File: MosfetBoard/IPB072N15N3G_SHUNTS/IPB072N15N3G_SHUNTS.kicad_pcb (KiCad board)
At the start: 2 copper layers, 147 x 97 mm, 116 parts, among them J1 DRIVER1, J13 BATT+Conn2, J14 BATT-Conn2, J15 PHASE_PAD, J16 PHASE_PAD, J2 DRIVER2, J3 DRIVER3, J4 PhaseConn1, J5 PhaseConn2, J6 PhaseConn3, J7 PHASE_PAD, J8 BATT+Conn1, J9 BATT-Conn1, Q1 IPB072N15N3G, Q10 IPB072N15N3G, Q11 IPB072N15N3G, Q12 IPB072N15N3G, Q2 IPB072N15N3G, Q3 IPB072N15N3G, Q4 IPB072N15N3G, Q5 IPB072N15N3G, Q6 IPB072N15N3G, Q7 IPB072N15N3G, Q8 IPB072N15N3G, Q9 IPB072N15N3G, U1 RS2166XC5, U4 NCS2003ASN2T1G, U5 RS2166XC5, U7 RS2166XC5, U8 NCS2003ASN2T1G, U9 NCS2003ASN2T1G

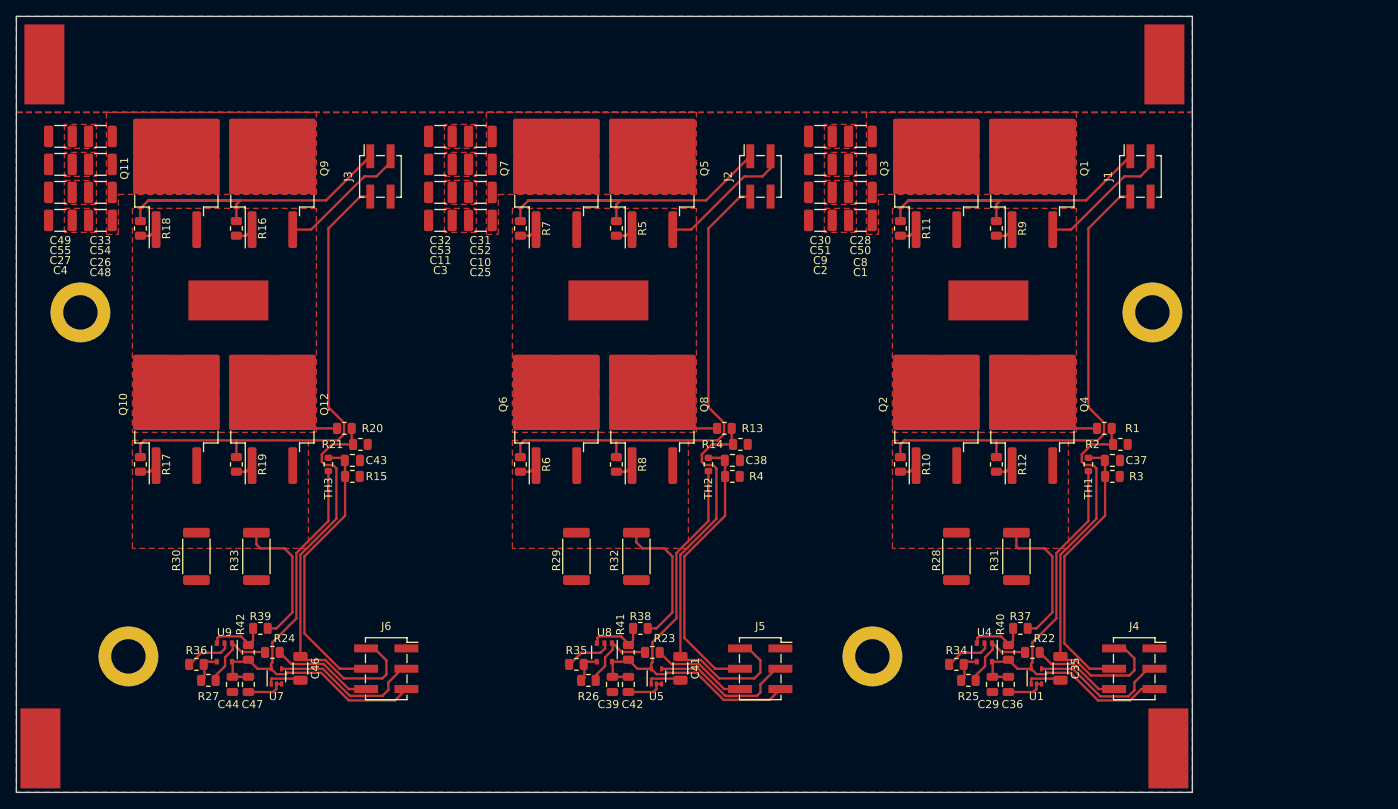
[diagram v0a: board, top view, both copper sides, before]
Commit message: fixing_giga_mistake
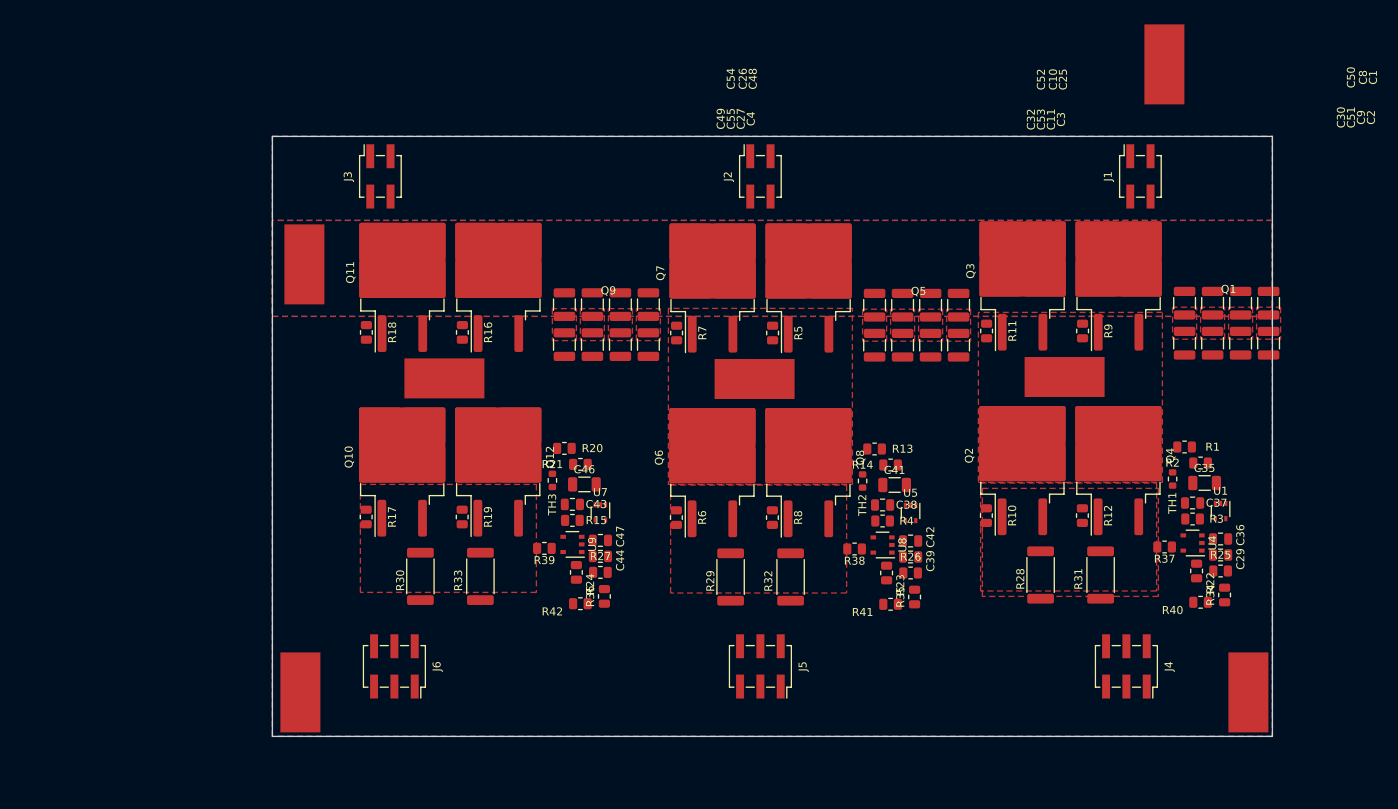
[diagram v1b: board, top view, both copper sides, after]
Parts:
- removed H1, H2, H3, H4: MountingHole, MountingHole:MountingHole_4.3mm_M4_DIN965_Pad
- J2: value DRIVER2 -> DRIVER1
- J3: value DRIVER3 -> DRIVER1
- J4: value PhaseConn1 -> PhaseConn
- J5: value PhaseConn2 -> PhaseConn
- J6: value PhaseConn3 -> PhaseConn
- moved C4 75.1 mm to (142.0, 79.0), turned to -90 degrees
- moved C27 72.5 mm to (138.5, 79.0), turned to -90 degrees
- moved C55 70.2 mm to (135.0, 79.0), turned to -90 degrees
- moved C48 69.3 mm to (142.0, 74.0), turned to -90 degrees
- moved C49 68.2 mm to (131.5, 79.0), turned to -90 degrees
- moved C3 66.6 mm to (180.8, 79.1), turned to -90 degrees
- moved C26 66.5 mm to (138.5, 74.0), turned to -90 degrees
- moved C11 64.2 mm to (177.3, 79.1), turned to -90 degrees
- moved C54 63.9 mm to (135.0, 74.0), turned to -90 degrees
- moved C53 62.0 mm to (173.8, 79.1), turned to -90 degrees
- moved C33 61.7 mm to (131.5, 74.0), turned to -90 degrees
- moved C25 60.7 mm to (180.8, 74.1), turned to -90 degrees
- moved C32 60.2 mm to (170.3, 79.1), turned to -90 degrees
- moved C2 58.1 mm to (219.5, 78.8), turned to -90 degrees
- moved C10 58.0 mm to (177.3, 74.1), turned to -90 degrees
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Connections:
- net 3.3V_1 renamed /PhaseMosfets/3.3V_IN
- net 3.3V_2 renamed /PhaseMosfets1/3.3V_IN
- net 3.3V_3 renamed /PhaseMosfets2/3.3V_IN
- net CURR1 renamed /PhaseMosfets/CURRENT_SENSE
- net CURR2 renamed /PhaseMosfets1/CURRENT_SENSE
- net CURR3 renamed /PhaseMosfets2/CURRENT_SENSE
- net MOSTEMP1 renamed /PhaseMosfets/MOS_TEMP
- net MOSTEMP2 renamed /PhaseMosfets1/MOS_TEMP
- net MOSTEMP3 renamed /PhaseMosfets2/MOS_TEMP
- net PH1 renamed /PhaseMosfets/PH
- net PH2 renamed /PhaseMosfets1/PH
- net PH3 renamed /PhaseMosfets2/PH
- net PHASE1 renamed /PhaseMosfets/PHASE
- net PHASE2 renamed /PhaseMosfets1/PHASE
- net PHASE3 renamed /PhaseMosfets2/PHASE
- net PL1 renamed /PhaseMosfets/PL
- net PL2 renamed /PhaseMosfets1/PL
- net PL3 renamed /PhaseMosfets2/PL
- net SENS_FILTER_ENABLE1 renamed /PhaseMosfets/SENSE_FILTER_EN
- net SENS_FILTER_ENABLE2 renamed /PhaseMosfets1/SENSE_FILTER_EN
- net SENS_FILTER_ENABLE3 renamed /PhaseMosfets2/SENSE_FILTER_EN
- net VSENSE1 renamed /PhaseMosfets/V_SENSE
- net VSENSE2 renamed /PhaseMosfets1/V_SENSE
- net VSENSE3 renamed /PhaseMosfets2/V_SENSE
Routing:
- net /PhaseMosfets2/PL: track 63.0 -> 0.00 mm
- net /PhaseMosfets1/PL: track 63.0 -> 0.00 mm
- net /PhaseMosfets/PL: track 63.0 -> 0.00 mm
- net /PhaseMosfets2/3.3V_IN: track 56.3 -> 0.00 mm
- net /PhaseMosfets1/3.3V_IN: track 55.5 -> 0.00 mm
- net /PhaseMosfets/3.3V_IN: track 54.8 -> 0.00 mm
- net /PhaseMosfets2/V_SENSE: track 51.2 -> 0.00 mm
- net /PhaseMosfets1/V_SENSE: track 50.3 -> 0.00 mm
- net /PhaseMosfets/V_SENSE: track 49.3 -> 0.00 mm
- net /PhaseMosfets2/PH: track 47.3 -> 0.00 mm
- net /PhaseMosfets1/PH: track 47.3 -> 0.00 mm
- net /PhaseMosfets/PH: track 47.3 -> 0.00 mm
- net /PhaseMosfets1/MOS_TEMP: track 35.8 -> 0.00 mm
- net /PhaseMosfets2/MOS_TEMP: track 35.5 -> 0.00 mm
- net /PhaseMosfets/MOS_TEMP: track 33.7 -> 0.00 mm
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- removed copper zone on F.Cu, net /PhaseMosfets2/PHASE
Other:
- board size 147 x 97 mm -> 125 x 75 mm

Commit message: fixeddimensions
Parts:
- moved C28 14.2 mm to (208.8, 88.0), turned to 0 degrees
- moved C33 14.1 mm to (133.0, 88.0), turned to 0 degrees
- moved C31 13.9 mm to (169.8, 88.0), turned to 0 degrees
- moved C25 11.5 mm to (169.8, 77.5), turned to 0 degrees
- moved C1 11.4 mm to (208.8, 77.5), turned to 0 degrees
- moved C50 11.3 mm to (208.8, 84.5), turned to 0 degrees
- moved C52 11.2 mm to (169.8, 84.5), turned to 0 degrees
- moved C49 11.1 mm to (138.0, 88.0), turned to 0 degrees
- moved C54 10.7 mm to (133.0, 84.5), turned to 0 degrees
- moved C30 10.3 mm to (213.8, 88.0), turned to 0 degrees
- moved C10 10.2 mm to (169.8, 81.0), turned to 0 degrees
- moved C8 10.2 mm to (208.8, 81.0), turned to 0 degrees
- moved C32 9.96 mm to (174.8, 88.0), turned to 0 degrees
- moved C48 9.65 mm to (133.0, 77.5), turned to 0 degrees
- moved C26 8.88 mm to (133.0, 81.0), turned to 0 degrees
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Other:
- board size 125 x 75 mm -> 115 x 75 mm

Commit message: movedconnectors
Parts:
- moved J13 29.1 mm to (211.2, 72.8)
- moved Q1 7.91 mm to (192.5, 74.5)
- moved R9 7.91 mm to (188.0, 82.0)
- moved Q4 7.70 mm to (192.5, 97.2)
- moved R12 7.70 mm to (188.0, 104.8)
- moved R30 7.60 mm to (119.0, 113.2)
- moved C50 7.59 mm to (201.5, 86.8)
- moved C2 7.59 mm to (206.5, 79.8)
- moved C30 7.59 mm to (206.5, 90.2)
- moved C51 7.59 mm to (206.5, 86.8)
- moved C8 7.59 mm to (201.5, 83.2)
- moved C9 7.59 mm to (206.5, 83.2)
- moved C28 7.59 mm to (201.5, 90.2)
- moved C1 7.59 mm to (201.5, 79.8)
- moved Q3 7.50 mm to (181.0, 74.5)
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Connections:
- C29 pad 1: /PhaseMosfets/3.3V_IN -> /PhaseMosfets1/3.3V_IN
- C35 pad 1: /PhaseMosfets/V_SENSE -> /PhaseMosfets1/V_SENSE
- C36 pad 1: /PhaseMosfets/3.3V_IN -> /PhaseMosfets1/3.3V_IN
- C37 pad 1: /PhaseMosfets/MOS_TEMP -> /PhaseMosfets1/MOS_TEMP
- C38 pad 1: /PhaseMosfets1/MOS_TEMP -> /PhaseMosfets2/MOS_TEMP
- C39 pad 1: /PhaseMosfets1/3.3V_IN -> /PhaseMosfets2/3.3V_IN
- C41 pad 1: /PhaseMosfets1/V_SENSE -> /PhaseMosfets2/V_SENSE
- C42 pad 1: /PhaseMosfets1/3.3V_IN -> /PhaseMosfets2/3.3V_IN
- C43 pad 1: /PhaseMosfets2/MOS_TEMP -> /PhaseMosfets3/MOS_TEMP
- C44 pad 1: /PhaseMosfets2/3.3V_IN -> /PhaseMosfets3/3.3V_IN
- C46 pad 1: /PhaseMosfets2/V_SENSE -> /PhaseMosfets3/V_SENSE
- C47 pad 1: /PhaseMosfets2/3.3V_IN -> /PhaseMosfets3/3.3V_IN
- J1 pad 1: /PhaseMosfets/PH -> /PhaseMosfets1/PH
- J1 pad 2: /PhaseMosfets/PL -> /PhaseMosfets1/PL
- J1 pad 3: /PhaseMosfets/PHASE -> /PhaseMosfets1/PHASE
- J15 pad 1: /PhaseMosfets1/PHASE -> /PhaseMosfets2/PHASE
- J16 pad 1: /PhaseMosfets2/PHASE -> /PhaseMosfets3/PHASE
- J2 pad 1: /PhaseMosfets1/PH -> /PhaseMosfets2/PH
- J2 pad 2: /PhaseMosfets1/PL -> /PhaseMosfets2/PL
- J2 pad 3: /PhaseMosfets1/PHASE -> /PhaseMosfets2/PHASE
- J3 pad 1: /PhaseMosfets2/PH -> /PhaseMosfets3/PH
- J3 pad 2: /PhaseMosfets2/PL -> /PhaseMosfets3/PL
- J3 pad 3: /PhaseMosfets2/PHASE -> /PhaseMosfets3/PHASE
- J4 pad 2: /PhaseMosfets/V_SENSE -> /PhaseMosfets1/V_SENSE
- J4 pad 3: /PhaseMosfets/SENSE_FILTER_EN -> /PhaseMosfets1/SENSE_FILTER_EN
- J4 pad 4: /PhaseMosfets/MOS_TEMP -> /PhaseMosfets1/MOS_TEMP
- J4 pad 5: /PhaseMosfets/3.3V_IN -> /PhaseMosfets1/3.3V_IN
- J4 pad 6: /PhaseMosfets/CURRENT_SENSE -> /PhaseMosfets1/CURRENT_SENSE
- J5 pad 2: /PhaseMosfets1/V_SENSE -> /PhaseMosfets2/V_SENSE
- J5 pad 3: /PhaseMosfets1/SENSE_FILTER_EN -> /PhaseMosfets2/SENSE_FILTER_EN
- J5 pad 4: /PhaseMosfets1/MOS_TEMP -> /PhaseMosfets2/MOS_TEMP
- J5 pad 5: /PhaseMosfets1/3.3V_IN -> /PhaseMosfets2/3.3V_IN
- J5 pad 6: /PhaseMosfets1/CURRENT_SENSE -> /PhaseMosfets2/CURRENT_SENSE
- J6 pad 2: /PhaseMosfets2/V_SENSE -> /PhaseMosfets3/V_SENSE
- J6 pad 3: /PhaseMosfets2/SENSE_FILTER_EN -> /PhaseMosfets3/SENSE_FILTER_EN
- J6 pad 4: /PhaseMosfets2/MOS_TEMP -> /PhaseMosfets3/MOS_TEMP
- J6 pad 5: /PhaseMosfets2/3.3V_IN -> /PhaseMosfets3/3.3V_IN
- J6 pad 6: /PhaseMosfets2/CURRENT_SENSE -> /PhaseMosfets3/CURRENT_SENSE
- J7 pad 1: /PhaseMosfets/PHASE -> /PhaseMosfets1/PHASE
- Q1 pad 3: /PhaseMosfets/PHASE -> /PhaseMosfets1/PHASE
- Q10 pad 2: /PhaseMosfets2/PHASE -> /PhaseMosfets3/PHASE
- Q10 pad 3: /PhaseMosfets2/SH+ -> /PhaseMosfets3/SH+
- Q11 pad 3: /PhaseMosfets2/PHASE -> /PhaseMosfets3/PHASE
- Q12 pad 2: /PhaseMosfets2/PHASE -> /PhaseMosfets3/PHASE
- Q12 pad 3: /PhaseMosfets2/SH+ -> /PhaseMosfets3/SH+
- Q2 pad 2: /PhaseMosfets/PHASE -> /PhaseMosfets1/PHASE
- Q2 pad 3: /PhaseMosfets/SH+ -> /PhaseMosfets1/SH+
- Q3 pad 3: /PhaseMosfets/PHASE -> /PhaseMosfets1/PHASE
- Q4 pad 2: /PhaseMosfets/PHASE -> /PhaseMosfets1/PHASE
- Q4 pad 3: /PhaseMosfets/SH+ -> /PhaseMosfets1/SH+
- Q5 pad 3: /PhaseMosfets1/PHASE -> /PhaseMosfets2/PHASE
- Q6 pad 2: /PhaseMosfets1/PHASE -> /PhaseMosfets2/PHASE
- Q6 pad 3: /PhaseMosfets1/SH+ -> /PhaseMosfets2/SH+
- Q7 pad 3: /PhaseMosfets1/PHASE -> /PhaseMosfets2/PHASE
- Q8 pad 2: /PhaseMosfets1/PHASE -> /PhaseMosfets2/PHASE
- Q8 pad 3: /PhaseMosfets1/SH+ -> /PhaseMosfets2/SH+
- Q9 pad 3: /PhaseMosfets2/PHASE -> /PhaseMosfets3/PHASE
- R1 pad 1: /PhaseMosfets/PHASE -> /PhaseMosfets1/PHASE
- R1 pad 2: /PhaseMosfets/V_SENSE -> /PhaseMosfets1/V_SENSE
- R10 pad 1: /PhaseMosfets/PL -> /PhaseMosfets1/PL
- R11 pad 1: /PhaseMosfets/PH -> /PhaseMosfets1/PH
- R12 pad 1: /PhaseMosfets/PL -> /PhaseMosfets1/PL
- R13 pad 1: /PhaseMosfets1/PHASE -> /PhaseMosfets2/PHASE
- R13 pad 2: /PhaseMosfets1/V_SENSE -> /PhaseMosfets2/V_SENSE
- R14 pad 1: /PhaseMosfets1/V_SENSE -> /PhaseMosfets2/V_SENSE
- R15 pad 1: /PhaseMosfets2/MOS_TEMP -> /PhaseMosfets3/MOS_TEMP
- R16 pad 1: /PhaseMosfets2/PH -> /PhaseMosfets3/PH
- R17 pad 1: /PhaseMosfets2/PL -> /PhaseMosfets3/PL
- R18 pad 1: /PhaseMosfets2/PH -> /PhaseMosfets3/PH
- R19 pad 1: /PhaseMosfets2/PL -> /PhaseMosfets3/PL
- R2 pad 1: /PhaseMosfets/V_SENSE -> /PhaseMosfets1/V_SENSE
- R20 pad 1: /PhaseMosfets2/PHASE -> /PhaseMosfets3/PHASE
- R20 pad 2: /PhaseMosfets2/V_SENSE -> /PhaseMosfets3/V_SENSE
- R21 pad 1: /PhaseMosfets2/V_SENSE -> /PhaseMosfets3/V_SENSE
- R22 pad 2: /PhaseMosfets/CURRENT_SENSE -> /PhaseMosfets1/CURRENT_SENSE
- R23 pad 2: /PhaseMosfets1/CURRENT_SENSE -> /PhaseMosfets2/CURRENT_SENSE
- R24 pad 2: /PhaseMosfets2/CURRENT_SENSE -> /PhaseMosfets3/CURRENT_SENSE
- R28 pad 1: /PhaseMosfets/SH+ -> /PhaseMosfets1/SH+
- R29 pad 1: /PhaseMosfets1/SH+ -> /PhaseMosfets2/SH+
- R3 pad 1: /PhaseMosfets/MOS_TEMP -> /PhaseMosfets1/MOS_TEMP
- R30 pad 1: /PhaseMosfets2/SH+ -> /PhaseMosfets3/SH+
- R31 pad 1: /PhaseMosfets/SH+ -> /PhaseMosfets1/SH+
- R32 pad 1: /PhaseMosfets1/SH+ -> /PhaseMosfets2/SH+
- R33 pad 1: /PhaseMosfets2/SH+ -> /PhaseMosfets3/SH+
- R37 pad 1: /PhaseMosfets/SH+ -> /PhaseMosfets1/SH+
- R38 pad 1: /PhaseMosfets1/SH+ -> /PhaseMosfets2/SH+
- R39 pad 1: /PhaseMosfets2/SH+ -> /PhaseMosfets3/SH+
- R4 pad 1: /PhaseMosfets1/MOS_TEMP -> /PhaseMosfets2/MOS_TEMP
- R40 pad 1: /PhaseMosfets/3.3V_IN -> /PhaseMosfets1/3.3V_IN
- R41 pad 1: /PhaseMosfets1/3.3V_IN -> /PhaseMosfets2/3.3V_IN
- R42 pad 1: /PhaseMosfets2/3.3V_IN -> /PhaseMosfets3/3.3V_IN
- R5 pad 1: /PhaseMosfets1/PH -> /PhaseMosfets2/PH
- R6 pad 1: /PhaseMosfets1/PL -> /PhaseMosfets2/PL
- R7 pad 1: /PhaseMosfets1/PH -> /PhaseMosfets2/PH
- R8 pad 1: /PhaseMosfets1/PL -> /PhaseMosfets2/PL
- R9 pad 1: /PhaseMosfets/PH -> /PhaseMosfets1/PH
- TH1 pad 1: /PhaseMosfets/3.3V_IN -> /PhaseMosfets1/3.3V_IN
- TH1 pad 2: /PhaseMosfets/MOS_TEMP -> /PhaseMosfets1/MOS_TEMP
- TH2 pad 1: /PhaseMosfets1/3.3V_IN -> /PhaseMosfets2/3.3V_IN
- TH2 pad 2: /PhaseMosfets1/MOS_TEMP -> /PhaseMosfets2/MOS_TEMP
- TH3 pad 1: /PhaseMosfets2/3.3V_IN -> /PhaseMosfets3/3.3V_IN
- TH3 pad 2: /PhaseMosfets2/MOS_TEMP -> /PhaseMosfets3/MOS_TEMP
- U1 pad 4: /PhaseMosfets/SENSE_FILTER_EN -> /PhaseMosfets1/SENSE_FILTER_EN
- U1 pad 5: /PhaseMosfets/3.3V_IN -> /PhaseMosfets1/3.3V_IN
- U4 pad 5: /PhaseMosfets/3.3V_IN -> /PhaseMosfets1/3.3V_IN
- U5 pad 4: /PhaseMosfets1/SENSE_FILTER_EN -> /PhaseMosfets2/SENSE_FILTER_EN
- U5 pad 5: /PhaseMosfets1/3.3V_IN -> /PhaseMosfets2/3.3V_IN
- U7 pad 4: /PhaseMosfets2/SENSE_FILTER_EN -> /PhaseMosfets3/SENSE_FILTER_EN
- U7 pad 5: /PhaseMosfets2/3.3V_IN -> /PhaseMosfets3/3.3V_IN
- U8 pad 5: /PhaseMosfets1/3.3V_IN -> /PhaseMosfets2/3.3V_IN
- U9 pad 5: /PhaseMosfets2/3.3V_IN -> /PhaseMosfets3/3.3V_IN
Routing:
- net /PhaseMosfets2/PHASE: vias 0 -> 55
- net -BATT: vias 0 -> 7
- added copper zone on B.Cu, net /PhaseMosfets1/PHASE
- added copper zone on B.Cu, net /PhaseMosfets2/PHASE
- added copper zone on F.Cu, net /PhaseMosfets2/PHASE
- added copper zone on B.Cu, net /PhaseMosfets3/PHASE
- added copper zone on F.Cu, net /PhaseMosfets3/PHASE
- removed copper zone on F.Cu, net /PhaseMosfets/PHASE
- removed copper zone on F.Cu, net /PhaseMosfets/SH+
- removed copper zone on F.Cu, net /PhaseMosfets1/SH+

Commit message: cleanup
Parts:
- removed J13: BATT+Conn2, Connector_Wire:SolderWirePad_1x01_SMD_5x10mm
- removed J8: BATT+Conn1, Connector_Wire:SolderWirePad_1x01_SMD_5x10mm
- C29, C36, C37, C38, C39, C42, C43, C44, C47: footprint Capacitor_SMD:C_0805_2012Metric -> GigaVescLibs:C_0603_1608Metric_L
- C35, C41, C46: footprint Capacitor_SMD:C_1206_3216Metric -> GigaVescLibs:C_0603_1608Metric_L
- R1, R13, R14, R15, R2, R20, R21, R22, R23, R24, R25, R26, R27, R3, R34, R35, R36, R37, R38, R39, R4, R40, R41, R42: footprint Resistor_SMD:R_0805_2012Metric -> Resistor_SMD:R_0603_1608Metric
- R10, R11, R12, R16, R17, R18, R19, R5, R6, R7, R8, R9: value 2r2 -> 2.2; footprint Resistor_SMD:R_0805_2012Metric -> Resistor_SMD:R_0603_1608Metric
- moved R40 10.0 mm to (203.8, 103.0)
- moved R41 10.0 mm to (169.0, 103.0)
- moved R42 10.0 mm to (134.2, 103.0)
- moved R29 8.31 mm to (145.5, 112.2)
- moved R32 8.31 mm to (149.5, 112.2)
- moved R34 6.08 mm to (200.0, 111.0)
- moved R35 6.08 mm to (165.2, 111.0)
- moved R36 6.08 mm to (130.5, 111.0)
- moved R25 4.88 mm to (200.7, 108.2), turned to 0 degrees
- moved R26 4.88 mm to (165.9, 108.2), turned to 0 degrees
- moved R27 4.88 mm to (131.2, 108.2), turned to 0 degrees
- moved U1 2.02 mm to (203.8, 100.5)
- moved U5 2.02 mm to (169.0, 100.5)
- moved U7 2.02 mm to (134.2, 100.5)
- moved R15 1.77 mm to (131.2, 101.2)
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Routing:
- net /PhaseMosfets3/PL: track 0.00 -> 90.8 mm, vias 0 -> 3
- net /PhaseMosfets2/PL: track 0.00 -> 77.3 mm, vias 0 -> 3
- net /PhaseMosfets3/PH: track 0.00 -> 63.7 mm, vias 0 -> 3
- net /PhaseMosfets1/PL: track 0.00 -> 62.8 mm, vias 0 -> 3
- net /PhaseMosfets3/3.3V_IN: track 0.00 -> 59.5 mm
- net /PhaseMosfets2/PH: track 0.00 -> 50.8 mm, vias 0 -> 3
- net /PhaseMosfets2/3.3V_IN: track 0.00 -> 48.7 mm
- net /PhaseMosfets3/PHASE: track 0.00 -> 46.7 mm, vias 0 -> 101
- net /PhaseMosfets1/PH: track 0.00 -> 44.9 mm, vias 0 -> 3
- net /PhaseMosfets3/SENSE_FILTER_EN: track 0.00 -> 43.7 mm, vias 0 -> 4
- net /PhaseMosfets1/3.3V_IN: track 0.00 -> 42.1 mm
- net /PhaseMosfets3/V_SENSE: track 0.00 -> 41.6 mm, vias 0 -> 4
- net /PhaseMosfets3/MOS_TEMP: track 0.00 -> 40.0 mm
- net /PhaseMosfets2/PHASE: track 0.00 -> 35.9 mm, vias 55 -> 101
- net /PhaseMosfets3/CURRENT_SENSE: track 0.00 -> 33.5 mm
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- added copper zone on B.Cu, net /PhaseMosfets1/SH+
- added copper zone on F.Cu, net /PhaseMosfets1/SH+
- added copper zone on B.Cu, net /PhaseMosfets2/SH+
- added copper zone on B.Cu, net /PhaseMosfets3/SH+
- added copper zone on F.Cu, net /PhaseMosfets3/SH+

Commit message: small changes
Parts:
- removed C29, C35, C36, C39, C41, C42, C44, C46, C47: 100nF, GigaVescLibs:C_0603_1608Metric_L
- removed R22, R23, R24: 150, Resistor_SMD:R_0603_1608Metric
- removed R25, R26, R27: 47k, Resistor_SMD:R_0603_1608Metric
- removed R34, R35, R36, R37, R38, R39: 2.2k, Resistor_SMD:R_0603_1608Metric
- removed R40, R41, R42: 100k, Resistor_SMD:R_0603_1608Metric
- removed U1, U5, U7: RS2166XC5, Package_TO_SOT_SMD:SOT-353_SC-70-5
- removed U4, U8, U9: NCS2003ASN2T1G, Package_SO:TSOP-5_1.65x3.05mm_P0.95mm
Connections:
- J4 pad 3: /PhaseMosfets1/SENSE_FILTER_EN -> /PhaseMosfets1/SH-
- J4 pad 6: /PhaseMosfets1/CURRENT_SENSE -> /PhaseMosfets1/SH+
- J5 pad 3: /PhaseMosfets2/SENSE_FILTER_EN -> /PhaseMosfets2/SH-
- J5 pad 6: /PhaseMosfets2/CURRENT_SENSE -> /PhaseMosfets2/SH+
- J6 pad 3: /PhaseMosfets3/SENSE_FILTER_EN -> /PhaseMosfets3/SH-
- J6 pad 6: /PhaseMosfets3/CURRENT_SENSE -> /PhaseMosfets3/SH+
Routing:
- net (no net): track 0.00 -> 54.9 mm
- net /PhaseMosfets3/SH-: track 0.00 -> 43.7 mm, vias 0 -> 4
- net /PhaseMosfets3/SENSE_FILTER_EN: track 43.7 -> 0.00 mm, vias 4 -> 0
- net /PhaseMosfets3/SH+: track 2.80 -> 36.3 mm
- net /PhaseMosfets3/CURRENT_SENSE: track 33.5 -> 0.00 mm
- net /PhaseMosfets2/SH-: track 0.00 -> 32.9 mm, vias 0 -> 4
- net /PhaseMosfets2/SENSE_FILTER_EN: track 32.9 -> 0.00 mm, vias 4 -> 0
- net /PhaseMosfets1/SH-: track 0.00 -> 27.1 mm, vias 0 -> 2
- net /PhaseMosfets1/SENSE_FILTER_EN: track 27.1 -> 0.00 mm, vias 2 -> 0
- net /PhaseMosfets2/SH+: track 2.80 -> 25.4 mm
- net /PhaseMosfets2/CURRENT_SENSE: track 22.6 -> 0.00 mm
- net /PhaseMosfets1/SH+: track 2.80 -> 11.7 mm, vias 28 -> 30
- net /PhaseMosfets1/CURRENT_SENSE: track 8.89 -> 0.00 mm, vias 2 -> 0
- net Net-(U9--): track 6.08 -> 0.00 mm
- net Net-(U8--): track 6.08 -> 0.00 mm
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
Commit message: v2.6.0 - cleanup
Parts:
- removed J15, J16, J7: PHASE_PAD, Connector_Wire:SolderWirePad_1x01_SMD_5x10mm
- added JP1: DummyJumper, GigaVescLibs:SolderJumper0.3mm, F.Cu at (194.0, 111.1)
- added JP2: DummyJumper, GigaVescLibs:SolderJumper0.3mm, F.Cu at (148.2, 111.1)
- added JP3: DummyJumper, GigaVescLibs:SolderJumper0.3mm, F.Cu at (102.5, 111.1)
- moved C1 27.8 mm to (229.2, 78.0), turned to -90 degrees
- moved C8 25.0 mm to (226.0, 78.0), turned to -90 degrees
- moved C2 23.2 mm to (229.2, 82.8), turned to -90 degrees
- moved C50 22.8 mm to (222.7, 78.0), turned to -90 degrees
- moved R15 22.8 mm to (108.5, 100.8), turned to -90 degrees
- moved R21 22.4 mm to (111.5, 100.8), turned to -90 degrees
- moved C28 21.4 mm to (219.5, 78.0), turned to -90 degrees
- moved C43 21.3 mm to (110.0, 100.8), turned to -90 degrees
- moved TH3 20.5 mm to (110.0, 97.8)
- moved R20 20.2 mm to (111.5, 97.8), turned to -90 degrees
- moved C9 19.8 mm to (226.0, 82.8), turned to -90 degrees
- moved Q4 17.8 mm to (209.5, 92.0)
- moved R12 17.6 mm to (205.0, 98.8)
- moved R31 17.3 mm to (209.5, 109.0)
- moved Q1 17.0 mm to (209.5, 74.0)
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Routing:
- net (no net): track 54.9 -> 0.00 mm
- net /PhaseMosfets3/3.3V_IN: track 59.5 -> 15.8 mm, vias 0 -> 2
- net /PhaseMosfets3/V_SENSE: track 41.6 -> 8.69 mm, vias 4 -> 2
- net /PhaseMosfets2/3.3V_IN: track 48.7 -> 15.8 mm, vias 0 -> 2
- net /PhaseMosfets3/SH-: track 43.7 -> 10.9 mm, vias 4 -> 0
- net /PhaseMosfets3/MOS_TEMP: track 40.0 -> 9.76 mm, vias 0 -> 2
- net /PhaseMosfets3/PL: track 90.8 -> 62.3 mm
- net /PhaseMosfets3/SH+: track 36.3 -> 9.23 mm, vias 28 -> 0
- net /PhaseMosfets3/PH: track 63.7 -> 37.0 mm
- net /PhaseMosfets1/3.3V_IN: track 42.1 -> 15.8 mm, vias 0 -> 2
- net -BATT: track 11.3 -> 33.6 mm, vias 108 -> 9
- net /PhaseMosfets2/SH-: track 32.9 -> 10.9 mm, vias 4 -> 0
- net /PhaseMosfets2/V_SENSE: track 30.5 -> 8.69 mm, vias 4 -> 2
- net /PhaseMosfets3/PHASE: track 46.7 -> 26.9 mm, vias 101 -> 2
- net /PhaseMosfets2/MOS_TEMP: track 29.0 -> 9.76 mm, vias 0 -> 2
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- removed copper zone on B.Cu, net /PhaseMosfets1/SH+
- removed copper zone on B.Cu, net /PhaseMosfets2/SH+
- removed copper zone on B.Cu, net /PhaseMosfets3/SH+
- removed copper zone on F.Cu, net Net-(C1-Pad2)
- removed copper zone on F.Cu, net Net-(C28-Pad2)
- removed copper zone on F.Cu, net Net-(C50-Pad2)
- removed copper zone on F.Cu, net Net-(C8-Pad2)
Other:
- board size 115 x 75 mm -> 120 x 75 mm

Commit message: v2.6.0 - cleanup
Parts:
- added REF**: TO-252-2, Package_TO_SOT_SMD:TO-252-2, F.Cu at (127.8, 95.8)
- moved R4 19.2 mm to (172.8, 95.5), turned to 0 degrees
- moved C38 18.3 mm to (172.8, 94.0), turned to 0 degrees
- moved TH2 15.4 mm to (170.5, 93.2)
- moved R14 13.8 mm to (171.0, 99.2)
- moved R13 13.3 mm to (170.5, 96.2)
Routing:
- net /PhaseMosfets2/3.3V_IN: track 15.8 -> 40.0 mm, vias 2 -> 0
- net /PhaseMosfets2/MOS_TEMP: track 9.76 -> 31.8 mm, vias 2 -> 0
- net /PhaseMosfets2/V_SENSE: track 8.69 -> 23.8 mm, vias 2 -> 0
- net -BATT: track 33.6 -> 22.4 mm, vias 9 -> 7
- net /PhaseMosfets2/PH: track 37.0 -> 29.4 mm, vias 3 -> 0
- net /PhaseMosfets2/PHASE: track 26.9 -> 34.5 mm, vias 2 -> 0
- net /PhaseMosfets2/PL: track 62.3 -> 65.6 mm, vias 3 -> 0
